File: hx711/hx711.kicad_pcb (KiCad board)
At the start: 2 copper layers, 55.9 x 43.2 mm, 8 parts, among them J1 Screw_Terminal_01x04, J2 Screw_Terminal_01x04, Q1 S8550, SW1 Rate Selector, U1 HX711

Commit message: made changes to the HX711 footprints and finihsed the pcb
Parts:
- Q1: footprint Package_TO_SOT_THT:TO-92_Inline -> Package_TO_SOT_SMD:TSOT-23
- SW1: footprint Button_Switch_SMD:SW_SPDT_CK-JS102011SAQN -> Button_Switch_SMD:SW_SPDT_PCM12
- moved Q1 6.19 mm to (139.4, 85.6), turned to 90 degrees
- moved SW1 0.49 mm to (141.5, 74.5)
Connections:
- net Net-(SW1A-B) renamed /rate
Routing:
- net Net-(Q1-B): track 20.3 -> 8.79 mm
- net +3.3V: track 115.6 -> 104.2 mm
- net /rate: track 20.1 -> 30.9 mm
- net GND: track 113.0 -> 118.2 mm
- net VCC: track 18.5 -> 16.2 mm

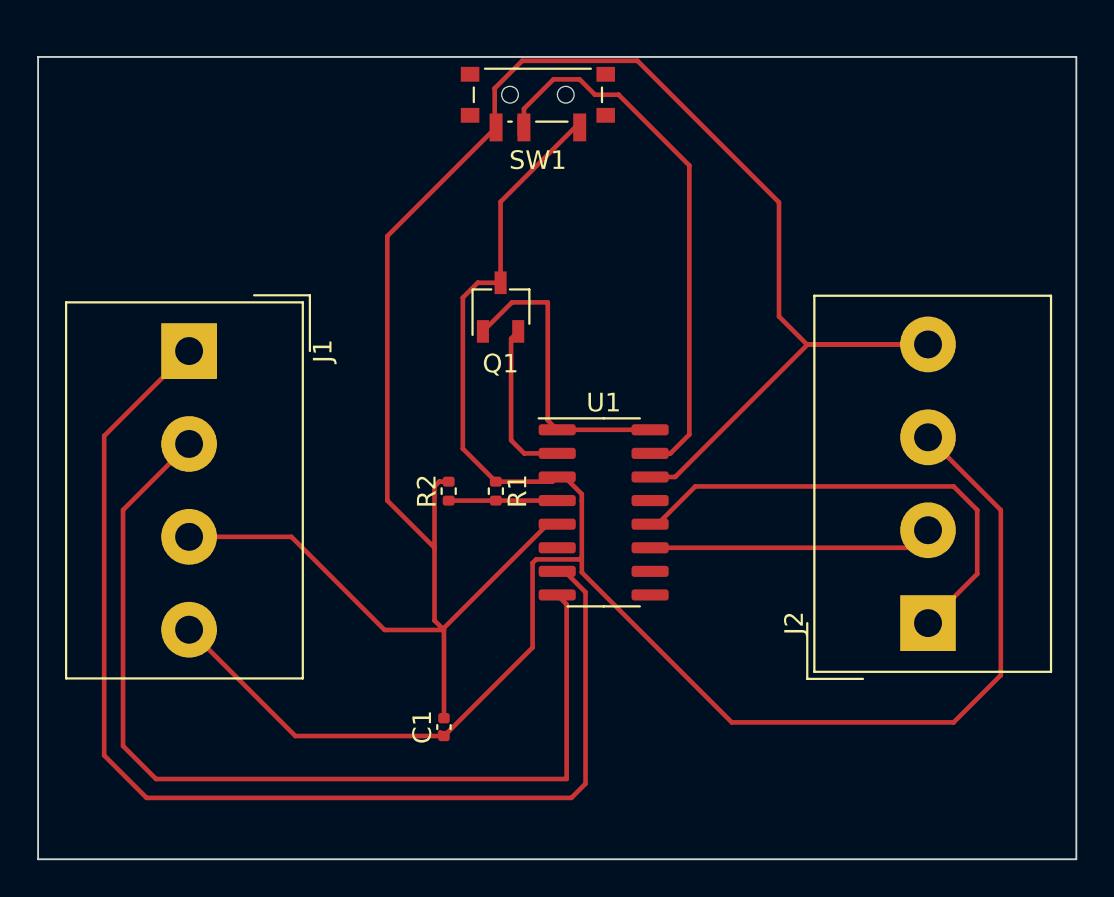
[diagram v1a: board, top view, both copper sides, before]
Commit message: Removed resistor at the ina- termina
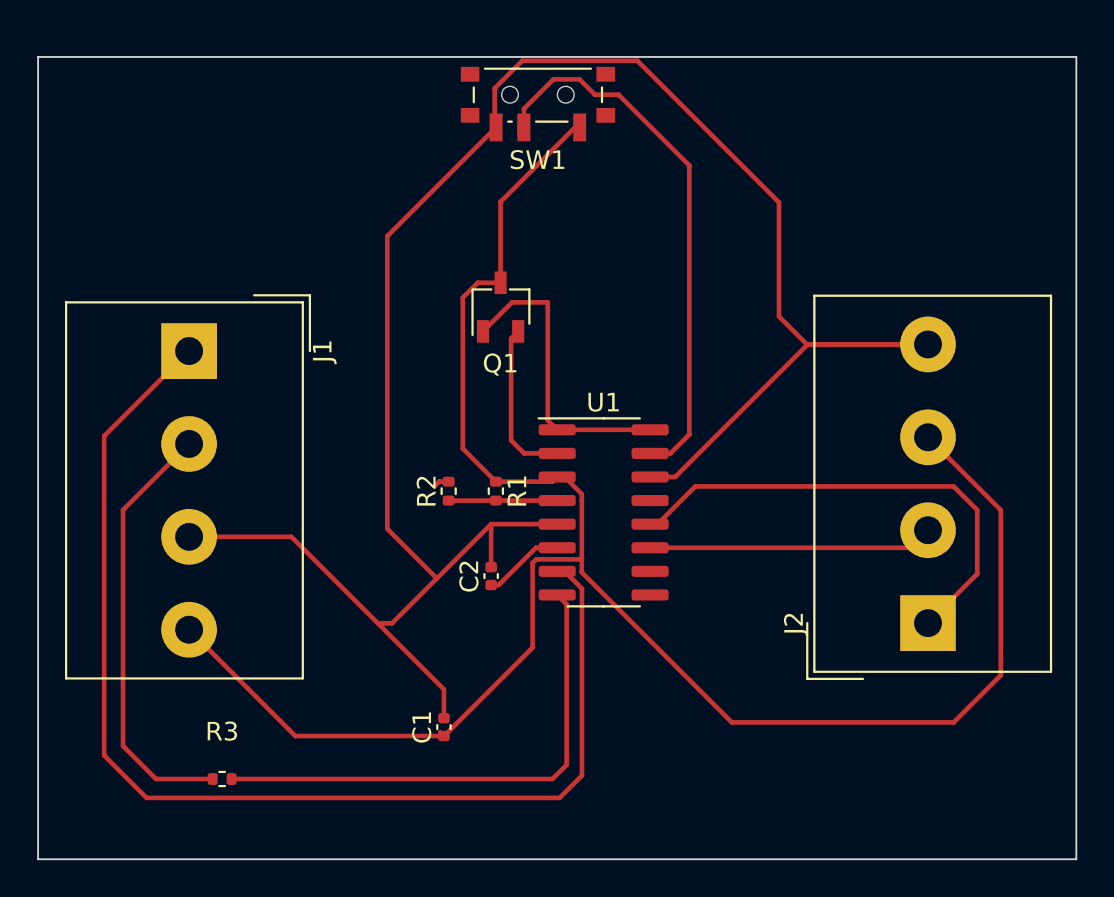
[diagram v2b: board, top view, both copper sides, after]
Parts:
- added C2: C, Capacitor_SMD:C_0402_1005Metric, F.Cu at (138.9, 100.1)
- added R3: R, Resistor_SMD:R_0402_1005Metric, F.Cu at (124.5, 111.0)
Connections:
- U1 pad 6: unconnected-(U1-VBG-Pad6) -> Net-(U1-VBG)
- U1 pad 8: Net-(J1-Pin_2) -> Net-(U1-INA+)
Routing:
- net Net-(J1-Pin_2): track 52.5 -> 23.3 mm
- net Net-(U1-INA+): track 0.00 -> 27.7 mm
- net Net-(U1-VBG): track 0.00 -> 4.39 mm
- net GND: track 118.2 -> 115.8 mm
- net Net-(J1-Pin_1): track 63.1 -> 62.6 mm
